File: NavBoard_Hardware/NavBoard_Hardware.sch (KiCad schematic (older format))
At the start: 51 parts, among them J1 Conn_Coaxial, U2 ATMEGA328P-Project_Library, U3 OKI, U4 OKI, U5 FGPMMOPA6H, Y1 Crystal

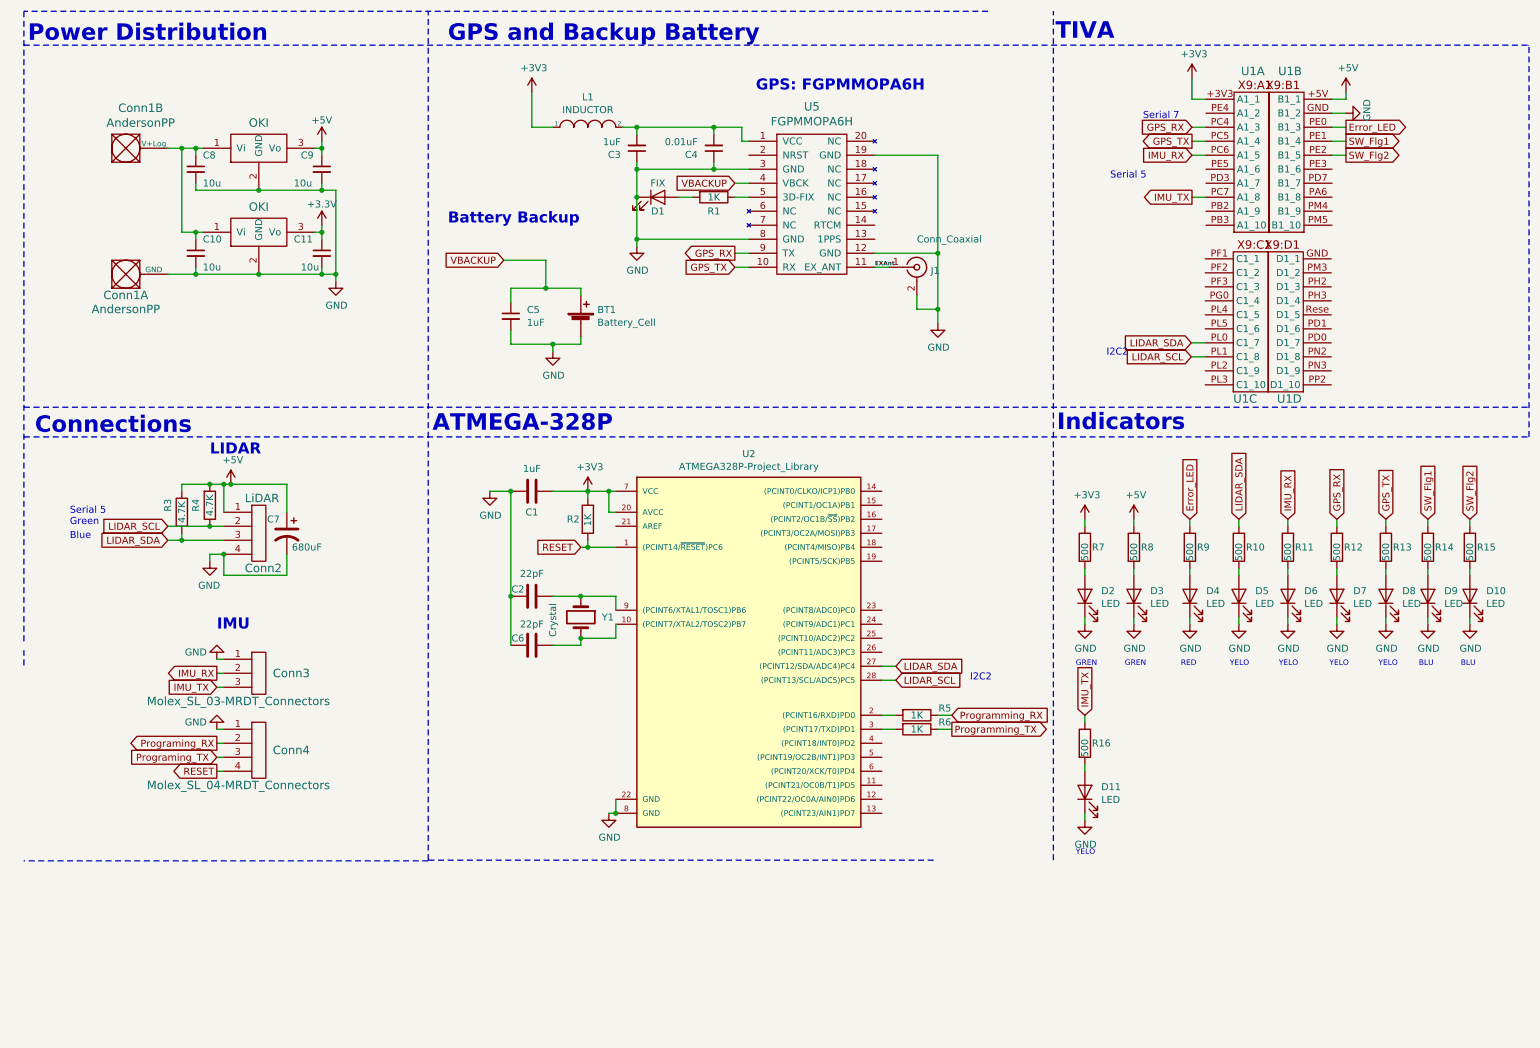
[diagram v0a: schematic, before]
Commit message: 3.3 to 5 volt converter added
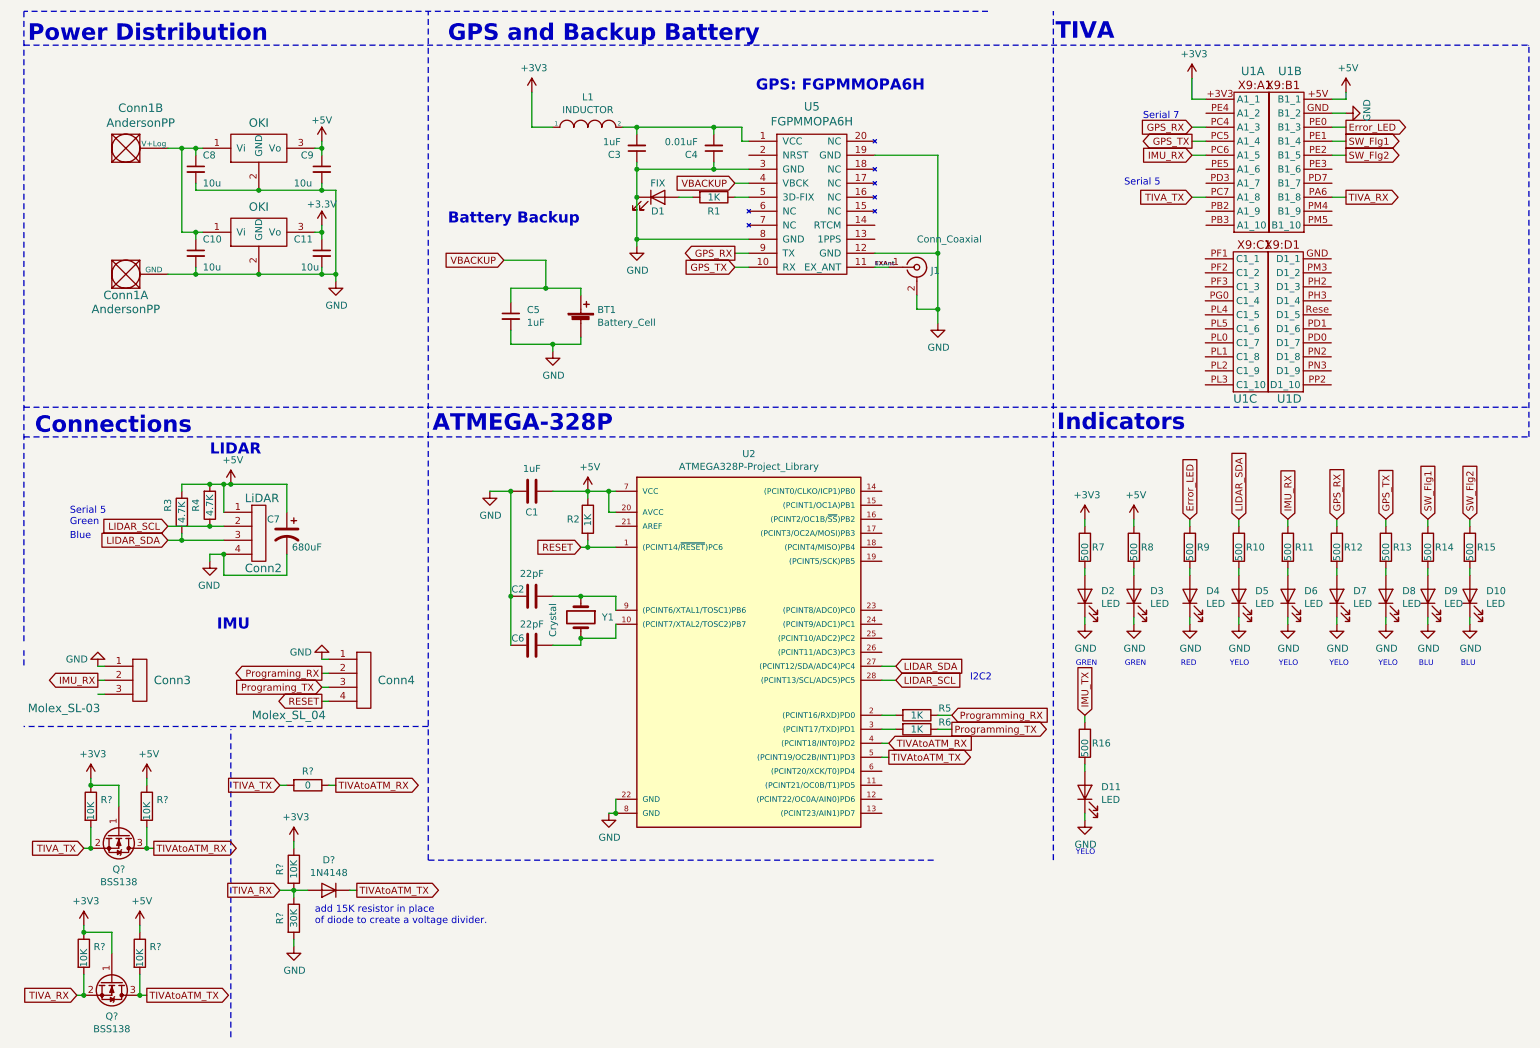
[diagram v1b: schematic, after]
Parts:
- added D?: 1N4148, Diode_THT:D_DO-35_SOD27_P7.62mm_Horizontal, symbol Diode:1N4148
- added Q? (x2): BSS138, Package_TO_SOT_SMD:SOT-23, symbol Transistor_FET:BSS138
- added R? (x5): 10K, symbol Device:R
- added R?: 0, symbol Device:R
- added R?: 30K, symbol Device:R
- Conn3: value Molex_SL_03-MRDT_Connectors -> Molex_SL-03
- Conn4: value Molex_SL_04-MRDT_Connectors -> Molex_SL_04
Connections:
- net +3V3: now also Q?.1 (G), Q?.1 (G), R?.1, R?.1, R?.1; no longer C1.1, R2.1, U2.20 (AVCC), U2.7 (VCC)
- net +5V: now also C1.1, R2.1, U2.20 (AVCC), U2.7 (VCC), R?.1, R?.1
- net GND: now also R?.2
- net IMU_TX: no longer Conn3.3, U1.PC7 (A1_8)
- net LIDAR_SCL: no longer U1.PL1 (C1_8)
- net LIDAR_SDA: no longer U1.PL0 (C1_7)
- net TIVA_RX: now reaches U1.PA6 (B1_8)
- net TIVA_RX: now also D?.2 (A), Q?.2 (S), R?.1, R?.2, R?.2
- net TIVAtoATM_RX: now reaches U2.4 ((PCINT18/INT0)PD2)
- net TIVAtoATM_RX: now also Q?.3 (D), R?.1, R?.2
- net TIVAtoATM_TX: now reaches U2.5 ((PCINT19/OC2B/INT1)PD3)
- net TIVAtoATM_TX: now also D?.1 (K), Q?.3 (D), R?.2
- new net TIVA_TX: Q?.2 (S), R?.2, R?.2, U1.PC7 (A1_8)
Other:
- note added: "add 15K resistor in place\nof diode to create a voltage divider.\n"
- moved on the sheet: Conn3, Conn4

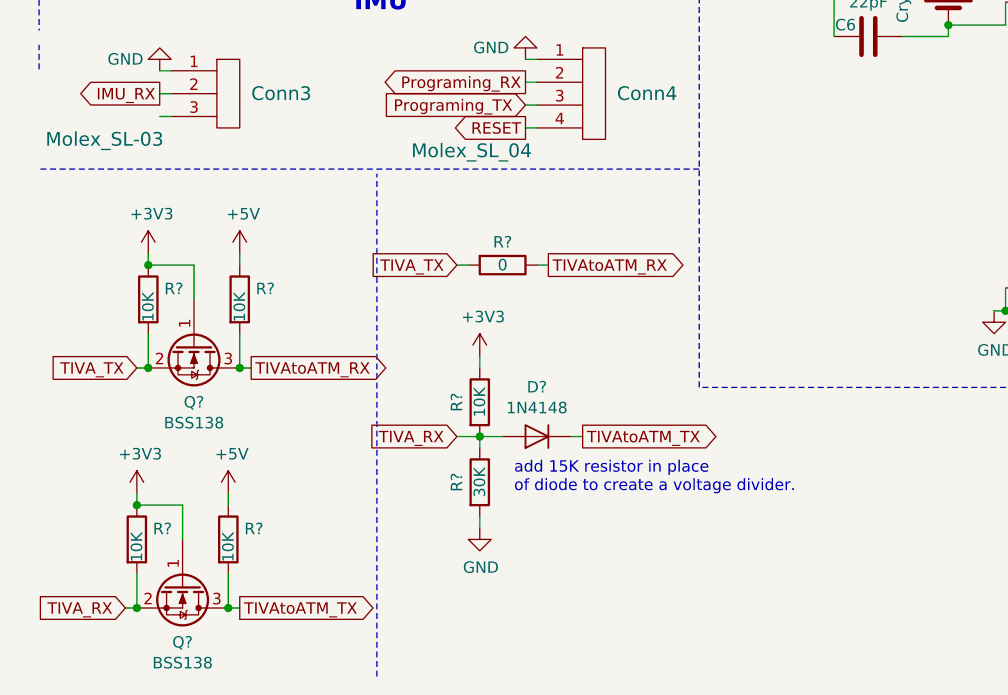
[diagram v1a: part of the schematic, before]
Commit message: added footprints
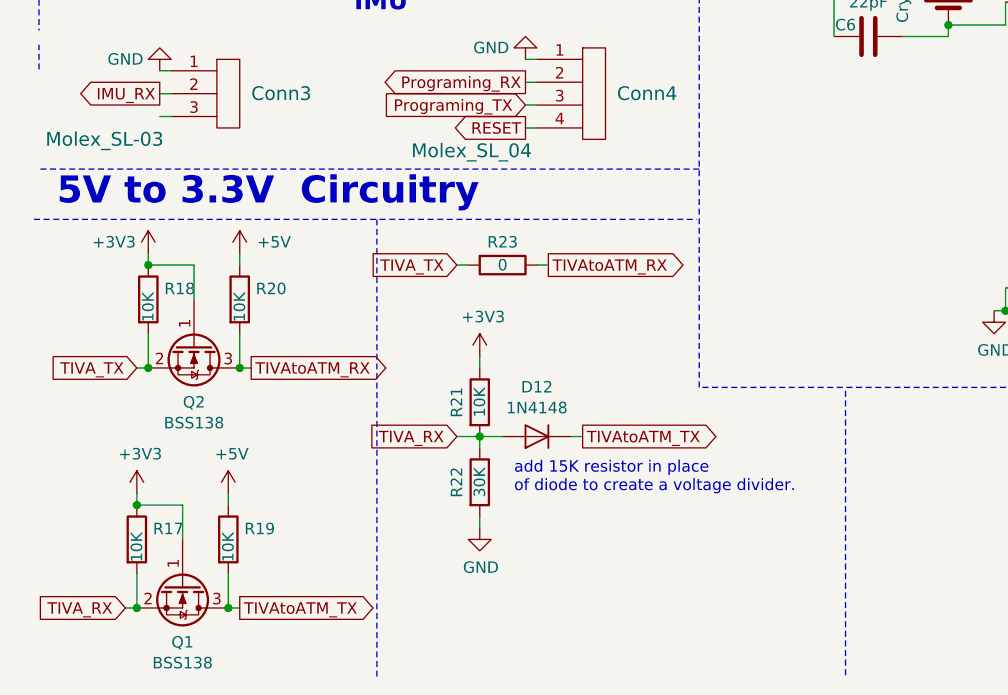
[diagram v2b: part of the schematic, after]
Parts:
- R17, R18, R19, R20, R21, R22, R23: renamed from R?; footprint (none) -> Resistor_SMD:R_0603_1608Metric_Pad1.05x0.95mm_HandSolder
- gave numbers to parts that had none: 3
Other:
- note added: "5V to 3.3V Circuitry"
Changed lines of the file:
@@
 	9915 1800 9815 1800
 $Comp
-L Device:R R?
+L Device:R R18
 U 1 1 5C8E176A
 P 950 6150
-F 0 "R?" H 1020 6196 50  0000 L CNN
+F 0 "R18" H 1020 6196 50  0000 L CNN
 F 1 "10K" V 950 6050 50  0000 L CNN
-F 2 "" V 880 6150 50  0001 C CNN
+F 2 "Resistor_SMD:R_0603_1608Metric_Pad1.05x0.95mm_HandSolder" V 880 6150 50  0001 C CNN
 F 3 "~" H 950 6150 50  0001 C CNN
 	1    950  6150
@@
 $EndComp
 $Comp
-L Device:R R?
+L Device:R R20
 U 1 1 5C8E1810
 P 1350 6150
-F 0 "R?" H 1420 6196 50  0000 L CNN
+F 0 "R20" H 1420 6196 50  0000 L CNN
 F 1 "10K" V 1350 6050 50  0000 L CNN
-F 2 "" V 1280 6150 50  0001 C CNN
+F 2 "Resistor_SMD:R_0603_1608Metric_Pad1.05x0.95mm_HandSolder" V 1280 6150 50  0001 C CNN
 F 3 "~" H 1350 6150 50  0001 C CNN
 	1    1350 6150
@@
 $EndComp
 $Comp
-L power:+3V3 #PWR?
+L power:+3V3 #PWR0130
 U 1 1 5C8F9600
 P 950 5950
-F 0 "#PWR?" H 950 5800 50  0001 C CNN
-F 1 "+3V3" H 965 6123 50  0000 C CNN
+F 0 "#PWR0130" H 950 5800 50  0001 C CNN
+F 1 "+3V3" H 800 6000 50  0000 C CNN
 F 2 "" H 950 5950 50  0001 C CNN
 F 3 "" H 950 5950 50  0001 C CNN
@@
 $EndComp
 $Comp
-L power:+5V #PWR?
+L power:+5V #PWR0131
 U 1 1 5C8F9697
 P 1350 5950
-F 0 "#PWR?" H 1350 5800 50  0001 C CNN
-F 1 "+5V" H 1365 6123 50  0000 C CNN
+F 0 "#PWR0131" H 1350 5800 50  0001 C CNN
+F 1 "+5V" H 1500 6000 50  0000 C CNN
 F 2 "" H 1350 5950 50  0001 C CNN
 F 3 "" H 1350 5950 50  0001 C CNN
@@
 $EndComp
 $Comp
-L Transistor_FET:BSS138 Q?
+L Transistor_FET:BSS138 Q2
 U 1 1 5C8F97FD
 P 1150 6350
-F 0 "Q?" V 1400 6350 50  0000 C CNN
+F 0 "Q2" V 1400 6350 50  0000 C CNN
 F 1 "BSS138" V 1491 6350 50  0000 C CNN
 F 2 "Package_TO_SOT_SMD:SOT-23" H 1350 6275 50  0001 L CIN
@@
 	1150 6000 1150 6150
 $Comp
-L Device:R R?
+L Device:R R17
 U 1 1 5C9E79FC
 P 900 7200
-F 0 "R?" H 970 7246 50  0000 L CNN
+F 0 "R17" H 970 7246 50  0000 L CNN
 F 1 "10K" V 900 7100 50  0000 L CNN
-F 2 "" V 830 7200 50  0001 C CNN
+F 2 "Resistor_SMD:R_0603_1608Metric_Pad1.05x0.95mm_HandSolder" V 830 7200 50  0001 C CNN
 F 3 "~" H 900 7200 50  0001 C CNN
 	1    900  7200
@@
 $EndComp
 $Comp
-L Device:R R?
+L Device:R R19
 U 1 1 5C9E7A03
 P 1300 7200
-F 0 "R?" H 1370 7246 50  0000 L CNN
+F 0 "R19" H 1370 7246 50  0000 L CNN
 F 1 "10K" V 1300 7100 50  0000 L CNN
-F 2 "" V 1230 7200 50  0001 C CNN
+F 2 "Resistor_SMD:R_0603_1608Metric_Pad1.05x0.95mm_HandSolder" V 1230 7200 50  0001 C CNN
 F 3 "~" H 1300 7200 50  0001 C CNN
 	1    1300 7200
@@
 $EndComp
 $Comp
-L power:+3V3 #PWR?
+L power:+3V3 #PWR0132
 U 1 1 5C9E7A0A
 P 900 7000
-F 0 "#PWR?" H 900 6850 50  0001 C CNN
+F 0 "#PWR0132" H 900 6850 50  0001 C CNN
 F 1 "+3V3" H 915 7173 50  0000 C CNN
 F 2 "" H 900 7000 50  0001 C CNN
@@
 $EndComp
 $Comp
-L power:+5V #PWR?
+L power:+5V #PWR0133
 U 1 1 5C9E7A10
 P 1300 7000
-F 0 "#PWR?" H 1300 6850 50  0001 C CNN
+F 0 "#PWR0133" H 1300 6850 50  0001 C CNN
 F 1 "+5V" H 1315 7173 50  0000 C CNN
 F 2 "" H 1300 7000 50  0001 C CNN
@@
 $EndComp
 $Comp
-L Transistor_FET:BSS138 Q?
+L Transistor_FET:BSS138 Q1
 U 1 1 5C9E7A16
 P 1100 7400
-F 0 "Q?" V 1350 7400 50  0000 C CNN
+F 0 "Q1" V 1350 7400 50  0000 C CNN
 F 1 "BSS138" V 1441 7400 50  0000 C CNN
 F 2 "Package_TO_SOT_SMD:SOT-23" H 1300 7325 50  0001 L CIN
@@
 Wire Wire Line
 	1100 7050 1100 7200
-Wire Notes Line
-	1950 7800 1950 5600
-$Comp
-L Device:R R?
+$Comp
+L Device:R R23
 U 1 1 5C9FA790
 P 2500 6000
-F 0 "R?" V 2400 6000 50  0000 C CNN
+F 0 "R23" V 2400 6000 50  0000 C CNN
 F 1 "0" V 2500 6000 50  0000 C CNN
-F 2 "" V 2430 6000 50  0001 C CNN
+F 2 "Resistor_SMD:R_0603_1608Metric_Pad1.05x0.95mm_HandSolder" V 2430 6000 50  0001 C CNN
 F 3 "~" H 2500 6000 50  0001 C CNN
 	1    2500 6000
@@
 TIVA_RX
 $Comp
-L Device:R R?
+L Device:R R22
 U 1 1 5CA440FD
 P 2400 6950
-F 0 "R?" V 2300 6950 50  0000 C CNN
+F 0 "R22" V 2300 6950 50  0000 C CNN
 F 1 "30K" V 2400 6950 50  0000 C CNN
-F 2 "" V 2330 6950 50  0001 C CNN
+F 2 "Resistor_SMD:R_0603_1608Metric_Pad1.05x0.95mm_HandSolder" V 2330 6950 50  0001 C CNN
 F 3 "~" H 2400 6950 50  0001 C CNN
 	1    2400 6950
@@
 $EndComp
 $Comp
-L power:GND #PWR?
+L power:GND #PWR0134
 U 1 1 5CA5FB60
 P 2400 7150
-F 0 "#PWR?" H 2400 6900 50  0001 C CNN
+F 0 "#PWR0134" H 2400 6900 50  0001 C CNN
 F 1 "GND" H 2405 6977 50  0000 C CNN
 F 2 "" H 2400 7150 50  0001 C CNN
@@
 	2400 7100 2400 7150
 $Comp
-L power:+3V3 #PWR?
+L power:+3V3 #PWR0135
 U 1 1 5CA7C380
 P 2400 6400
-F 0 "#PWR?" H 2400 6250 50  0001 C CNN
+F 0 "#PWR0135" H 2400 6250 50  0001 C CNN
 F 1 "+3V3" H 2415 6573 50  0000 C CNN
 F 2 "" H 2400 6400 50  0001 C CNN
@@
 $EndComp
 $Comp
-L Device:R R?
+L Device:R R21
 U 1 1 5CA7C418
 P 2400 6600
-F 0 "R?" V 2300 6600 50  0000 C CNN
+F 0 "R21" V 2300 6600 50  0000 C CNN
 F 1 "10K" V 2400 6600 50  0000 C CNN
-F 2 "" V 2330 6600 50  0001 C CNN
+F 2 "Resistor_SMD:R_0603_1608Metric_Pad1.05x0.95mm_HandSolder" V 2330 6600 50  0001 C CNN
 F 3 "~" H 2400 6600 50  0001 C CNN
 	1    2400 6600
@@
 	2400 6400 2400 6450
 $Comp
-L Diode:1N4148 D?
+L Diode:1N4148 D12
 U 1 1 5CAB5E96
 P 2650 6750
-F 0 "D?" H 2650 6534 50  0000 C CNN
+F 0 "D12" H 2650 6534 50  0000 C CNN
 F 1 "1N4148" H 2650 6625 50  0000 C CNN
 F 2 "Diode_THT:D_DO-35_SOD27_P7.62mm_Horizontal" H 2650 6575 50  0001 C CNN
@@
 Text Notes 2550 7000 0    50   ~ 0
 add 15K resistor in place\nof diode to create a voltage divider.\n
+Text Notes 550  5750 0    118  ~ 24
+5V to 3.3V  Circuitry
+Wire Notes Line
+	450  5800 3350 5800
+Wire Notes Line
+	1950 5800 1950 7800
+Wire Notes Line
+	4000 6550 4000 7800
 $EndSCHEMATC

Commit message: molex 2 added
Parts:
- Conn3: value Molex_SL-03 -> Molex_SL-02; footprint MRDT_Connectors:MOLEX_SL_03_Horizontal -> MRDT_Connectors:MOLEX_SL_02_Horizontal; symbol NavBoard_Hardware-rescue:Molex_SL_03-MRDT_Connectors -> MRDT_Connectors:Molex_SL_02
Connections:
- wire segments 188 -> 187
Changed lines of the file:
@@
 	10800 4800 10800 4850
 $Comp
-L NavBoard_Hardware-rescue:Molex_SL_03-MRDT_Connectors Conn3
+L MRDT_Connectors:Molex_SL_02 Conn3
 U 1 1 5C7D6386
 P 1250 5400
 F 0 "Conn3" H 1400 5550 60  0000 L CNN
-F 1 "Molex_SL-03" H 500 5350 60  0000 L CNN
-F 2 "MRDT_Connectors:MOLEX_SL_03_Horizontal" H 1250 5400 60  0001 C CNN
+F 1 "Molex_SL-02" H 500 5350 60  0000 L CNN
+F 2 "MRDT_Connectors:MOLEX_SL_02_Horizontal" H 1250 5400 60  0001 C CNN
 F 3 "" H 1250 5400 60  0001 C CNN
 	1    1250 5400
@@
 	1    0    0    -1
 $EndComp
-Text GLabel 1000 5250 0    50   Output ~ 0
+Text GLabel 1000 5350 0    50   Output ~ 0
 IMU_RX
-Wire Wire Line
-	1000 5150 1050 5150
-Wire Wire Line
-	1050 5250 1000 5250
 Wire Wire Line
 	1000 5350 1050 5350
@@
 L power:GND #PWR0127
 U 1 1 5C819482
-P 1000 5150
-F 0 "#PWR0127" H 1000 4900 50  0001 C CNN
-F 1 "GND" H 1150 5100 50  0000 C CNN
-F 2 "" H 1000 5150 50  0001 C CNN
-F 3 "" H 1000 5150 50  0001 C CNN
-	1    1000 5150
+P 1000 5250
+F 0 "#PWR0127" H 1000 5000 50  0001 C CNN
+F 1 "GND" H 1150 5200 50  0000 C CNN
+F 2 "" H 1000 5250 50  0001 C CNN
+F 3 "" H 1000 5250 50  0001 C CNN
+	1    1000 5250
 	-1   0    0    1
 $EndComp
@@
 Wire Notes Line
 	4000 6550 4000 7800
+Wire Wire Line
+	1050 5250 1000 5250
 $EndSCHEMATC

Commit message: Added level shifter to board and made traces beautiful
I, Andre did alot. I sleep now
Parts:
- removed D11: LED, LED_SMD:LED_0603_1608Metric_Pad1.05x0.95mm_HandSolder, symbol Device:LED
- removed R16: 500, Resistor_SMD:R_0603_1608Metric_Pad1.05x0.95mm_HandSolder, symbol Device:R
- Conn3: symbol MRDT_Connectors:Molex_SL_02 -> NavBoard_Hardware-rescue:Molex_SL_02-MRDT_Connectors
- D12: footprint Diode_THT:D_DO-35_SOD27_P7.62mm_Horizontal -> Diode_SMD:D_SOD-323
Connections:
- net labels removed: IMU_TX
- wire segments 187 -> 184
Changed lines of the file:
@@
 	10800 4800 10800 4850
 $Comp
-L MRDT_Connectors:Molex_SL_02 Conn3
+L NavBoard_Hardware-rescue:Molex_SL_02-MRDT_Connectors Conn3
 U 1 1 5C7D6386
 P 1250 5400
@@
 	1    0    0    -1
 $EndComp
-Text GLabel 1000 5350 0    50   Output ~ 0
+Text GLabel 1000 5250 0    50   Output ~ 0
 IMU_RX
 Wire Wire Line
-	1000 5350 1050 5350
+	1000 5250 1050 5250
 Text GLabel 2600 5200 0    50   Output ~ 0
 Programing_RX
@@
 L power:GND #PWR0127
 U 1 1 5C819482
-P 1000 5250
-F 0 "#PWR0127" H 1000 5000 50  0001 C CNN
-F 1 "GND" H 1150 5200 50  0000 C CNN
-F 2 "" H 1000 5250 50  0001 C CNN
-F 3 "" H 1000 5250 50  0001 C CNN
-	1    1000 5250
-	-1   0    0    1
+P 1000 5350
+F 0 "#PWR0127" H 1000 5100 50  0001 C CNN
+F 1 "GND" H 1150 5300 50  0000 C CNN
+F 2 "" H 1000 5350 50  0001 C CNN
+F 3 "" H 1000 5350 50  0001 C CNN
+	1    1000 5350
+	1    0    0    -1
 $EndComp
 $Comp
@@
 	-1   0    0    1
 $EndComp
-Text Notes 7985 6505 0    39   ~ 0
-YELO\n
-$Comp
-L Device:LED D11
-U 1 1 5C827458
-P 8050 6050
-F 0 "D11" V 8088 5933 50  0000 R CNN
-F 1 "LED" V 7997 5933 50  0000 R CNN
-F 2 "LED_SMD:LED_0603_1608Metric_Pad1.05x0.95mm_HandSolder" H 8050 6050 50  0001 C CNN
-F 3 "~" H 8050 6050 50  0001 C CNN
-	1    8050 6050
-	0    -1   -1   0
-$EndComp
-$Comp
-L Device:R R16
-U 1 1 5C82745F
-P 8050 5700
-F 0 "R16" H 8100 5700 50  0000 L CNN
-F 1 "500" V 8050 5600 50  0000 L CNN
-F 2 "Resistor_SMD:R_0603_1608Metric_Pad1.05x0.95mm_HandSolder" V 7980 5700 50  0001 C CNN
-F 3 "~" H 8050 5700 50  0001 C CNN
-	1    8050 5700
-	1    0    0    -1
-$EndComp
-Text GLabel 8050 5500 1    50   Input ~ 0
-IMU_TX
-Wire Wire Line
-	8050 5500 8050 5550
-Wire Wire Line
-	8050 5850 8050 5900
-$Comp
-L power:GND #PWR0129
-U 1 1 5C827469
-P 8050 6250
-F 0 "#PWR0129" H 8050 6000 50  0001 C CNN
-F 1 "GND" H 8055 6077 50  0000 C CNN
-F 2 "" H 8050 6250 50  0001 C CNN
-F 3 "" H 8050 6250 50  0001 C CNN
-	1    8050 6250
-	1    0    0    -1
-$EndComp
-Wire Wire Line
-	8050 6200 8050 6250
 Text GLabel 6650 5800 2    50   Output ~ 0
 TIVAtoATM_TX
@@
 F 0 "D12" H 2650 6534 50  0000 C CNN
 F 1 "1N4148" H 2650 6625 50  0000 C CNN
-F 2 "Diode_THT:D_DO-35_SOD27_P7.62mm_Horizontal" H 2650 6575 50  0001 C CNN
+F 2 "Diode_SMD:D_SOD-323" H 2650 6575 50  0001 C CNN
 F 3 "https://assets.nexperia.com/documents/data-sheet/1N4148_1N4448.pdf" H 2650 6750 50  0001 C CNN
 	1    2650 6750
@@
 	4000 6550 4000 7800
 Wire Wire Line
-	1050 5250 1000 5250
+	1050 5350 1000 5350
 $EndSCHEMATC
